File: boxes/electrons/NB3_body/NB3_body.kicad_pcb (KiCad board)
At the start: 2 copper layers, 200 x 199.5 mm, 18 parts, among them J1 Conn_02x05_Counter_Clockwise, J10 Conn_02x03_Top_Bottom, J11 Conn_02x03_Top_Bottom, J12 Conn_02x03_Top_Bottom, J13 JST ZH 6-way Socket, J14 JST ZH 6-way Socket, J2 Conn_02x05_Counter_Clockwise, J3 Conn_02x05_Counter_Clockwise, J4 Conn_02x05_Counter_Clockwise, J5 Conn_02x05_Counter_Clockwise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

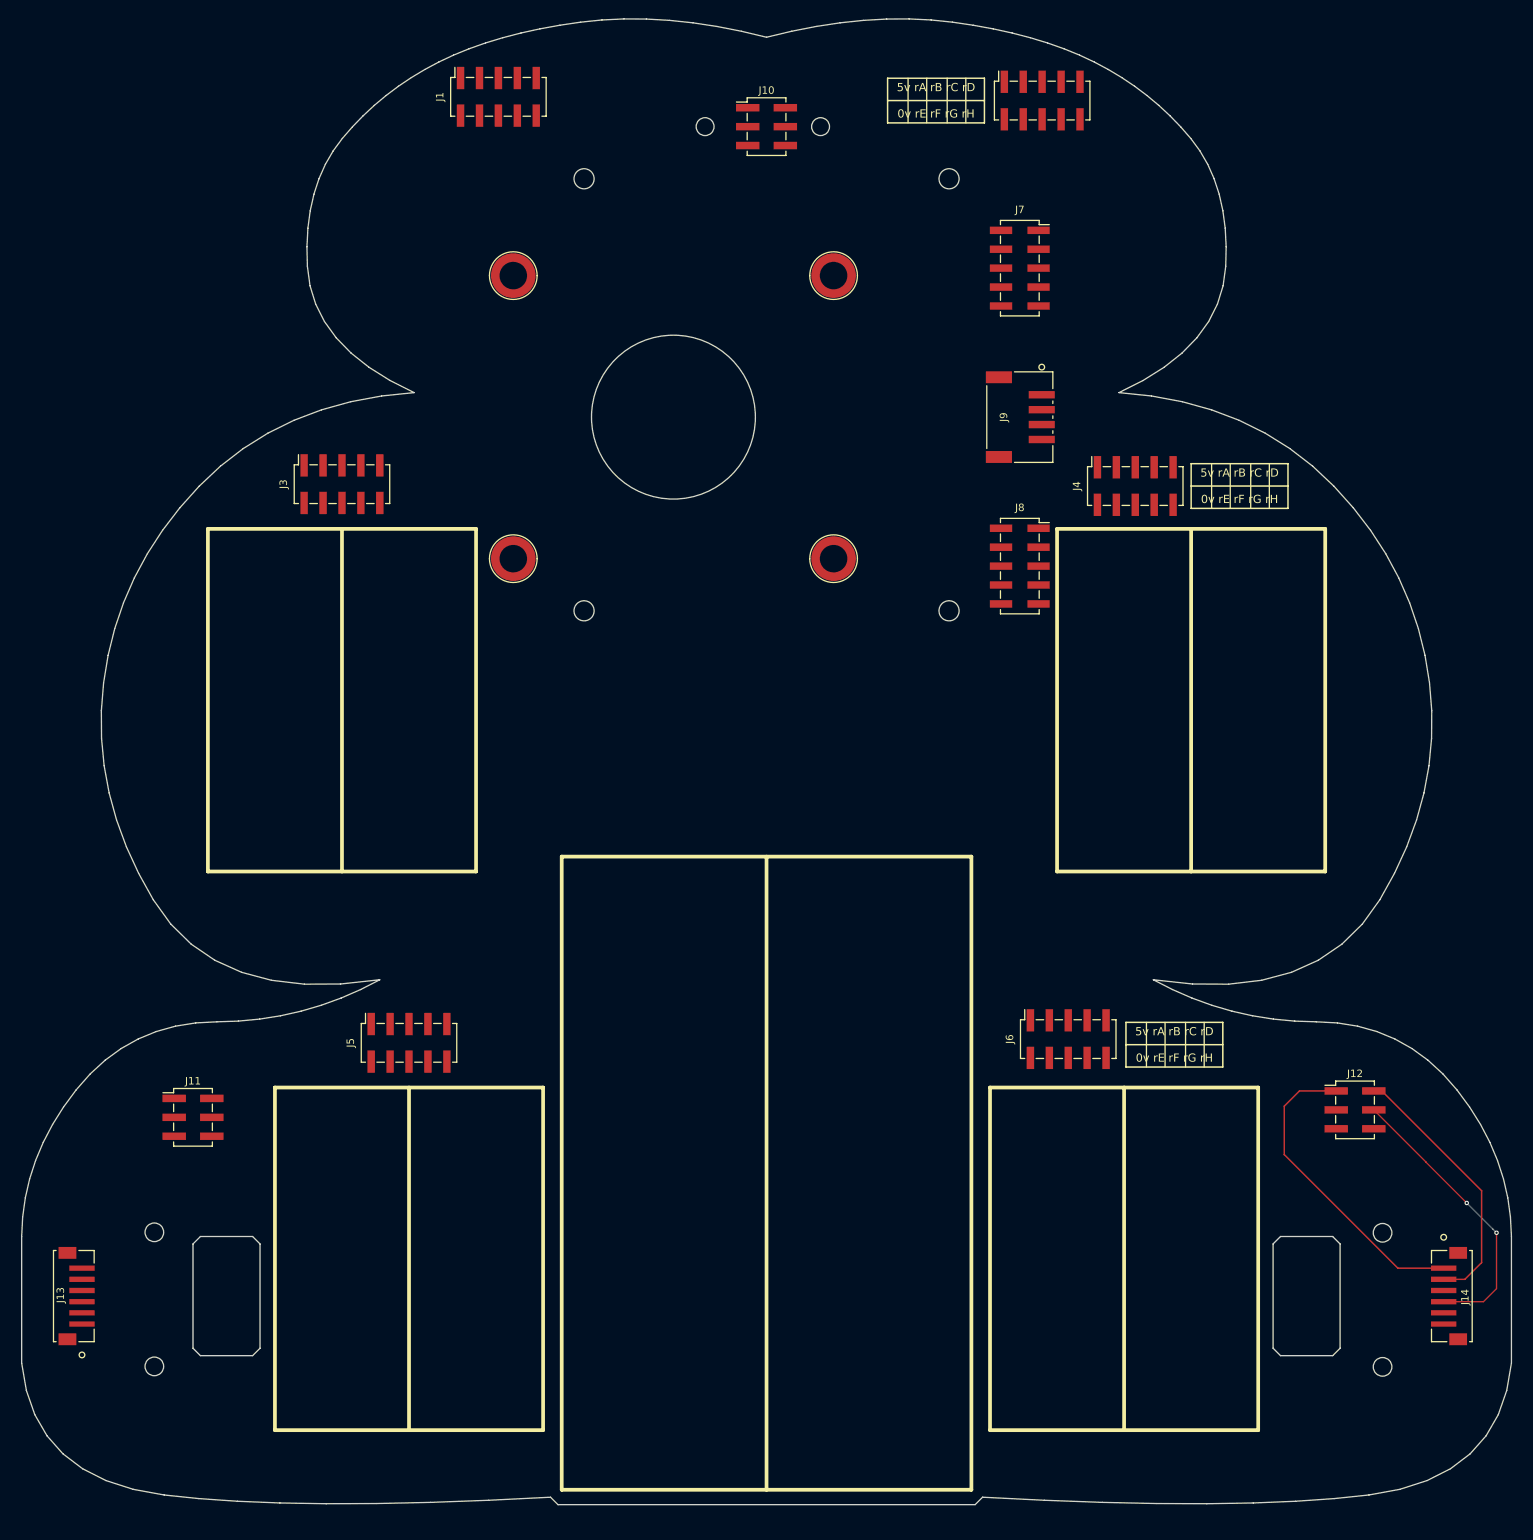
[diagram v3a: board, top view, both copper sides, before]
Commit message: NB3 pcb design tweaks
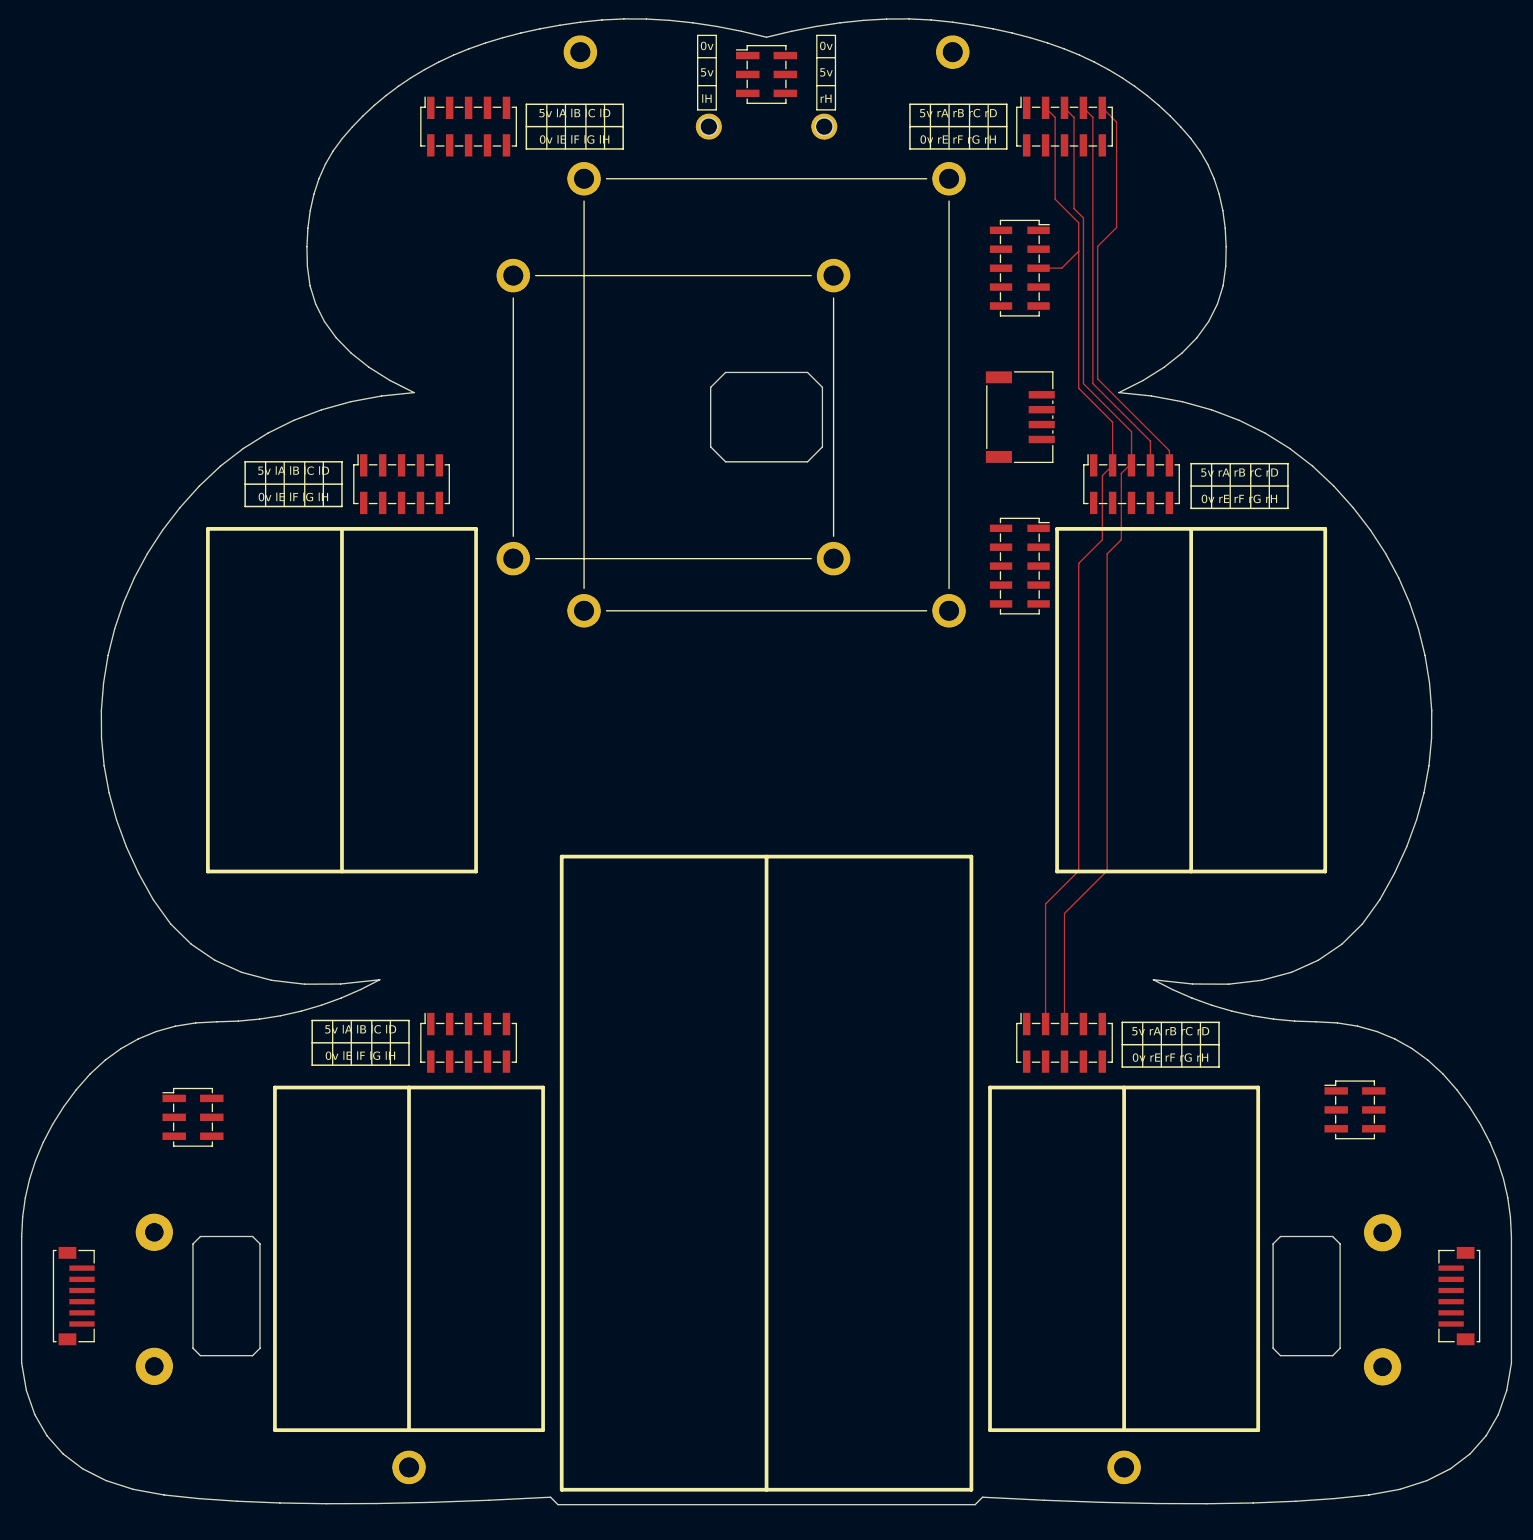
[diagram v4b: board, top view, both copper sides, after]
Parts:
- added H10: MountingHole, MountingHole:MountingHole_2.5mm_Pad, F.Cu at (207.2, 186.5)
- added H11: MountingHole, MountingHole:MountingHole_2.5mm_Pad, F.Cu at (42.3, 204.4)
- added H12: MountingHole, MountingHole:MountingHole_2.5mm_Pad, F.Cu at (207.2, 204.5)
- added H13: MountingHole, MountingHole:MountingHole_2.7mm_M2.5_ISO7380_Pad, F.Cu at (99.5, 28.0)
- added H14: MountingHole, MountingHole:MountingHole_2.7mm_M2.5_ISO7380_Pad, F.Cu at (149.5, 28.0)
- added H15: MountingHole, MountingHole:MountingHole_2.7mm_M2.5_ISO7380_Pad, F.Cu at (76.5, 218.0)
- added H16: MountingHole, MountingHole:MountingHole_2.7mm_M2.5_ISO7380_Pad, F.Cu at (172.5, 218.0)
- added H17: MountingHole, MountingHole:MountingHole_2.2mm_M2_ISO7380_Pad, F.Cu at (116.8, 38.0)
- added H18: MountingHole, MountingHole:MountingHole_2.2mm_M2_ISO7380_Pad, F.Cu at (132.2, 38.0)
- added H5: MountingHole, MountingHole:MountingHole_2.7mm_M2.5_ISO7380_Pad, F.Cu at (100.0, 45.0)
- added H6: MountingHole, MountingHole:MountingHole_2.7mm_M2.5_ISO7380_Pad, F.Cu at (149.0, 45.0)
- added H7: MountingHole, MountingHole:MountingHole_2.7mm_M2.5_ISO7380_Pad, F.Cu at (100.0, 103.0)
- added H8: MountingHole, MountingHole:MountingHole_2.7mm_M2.5_ISO7380_Pad, F.Cu at (149.0, 103.0)
- added H9: MountingHole, MountingHole:MountingHole_2.5mm_Pad, F.Cu at (42.3, 186.4)
- H1, H2, H3, H4: value Standoff_SMT_5H_M2.5_9774050151R -> MountingHole; footprint NB3_body:Standoff_SMT_5H_M2.5_9774050151R -> MountingHole:MountingHole_2.7mm_M2.5_ISO7380_Pad
- moved J3 8.00 mm to (75.5, 86.0)
- moved J5 8.00 mm to (84.5, 161.0)
- moved J10 7.00 mm to (124.5, 31.0)
- moved J1 5.66 mm to (84.5, 38.0)
- moved J2 4.61 mm to (164.5, 38.0)
- moved J14 1.00 mm to (217.5, 195.0)
- moved J6 0.71 mm to (164.5, 161.0)
- moved J4 0.56 mm to (173.5, 86.0)
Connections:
- J1 pad 10: GND -> /LH
- J1 pad 2: /LA -> GND
- J1 pad 3: /LB -> /LA
- J1 pad 4: /LC -> /LE
- J1 pad 5: /LD -> /LB
- J1 pad 6: /LH -> /LF
- J1 pad 7: /LG -> /LC
- J1 pad 8: /LF -> /LG
- J1 pad 9: /LE -> /LD
- J10 pad 2: +5V -> GND
- J10 pad 3: /LH -> +5V
- J10 pad 4: GND -> +5V
- J10 pad 5: +5V -> /LH
- J11 pad 2: /LE+ -> /LE B
- J11 pad 3: /LE A -> /LE+
- J11 pad 4: /LE B -> /LE-
- J11 pad 5: /LE- -> /LE A
- J12 pad 2: /RE+ -> /RE B
- J12 pad 3: /RE A -> /RE+
- J12 pad 4: /RE B -> /RE-
- J12 pad 5: /RE- -> /RE A
- J2 pad 10: GND -> /RH
- J2 pad 2: /RA -> GND
- J2 pad 3: /RB -> /RA
- J2 pad 4: /RC -> /RE
- J2 pad 5: /RD -> /RB
- J2 pad 6: /RH -> /RF
- J2 pad 7: /RG -> /RC
- J2 pad 8: /RF -> /RG
- J2 pad 9: /RE -> /RD
- J3 pad 10: GND -> /LH
- J3 pad 2: /LA -> GND
- J3 pad 3: /LB -> /LA
- J3 pad 4: /LC -> /LE
- J3 pad 5: /LD -> /LB
- J3 pad 6: /LH -> /LF
- J3 pad 7: /LG -> /LC
- J3 pad 8: /LF -> /LG
- J3 pad 9: /LE -> /LD
- J4 pad 10: GND -> /RH
- J4 pad 2: /RA -> GND
- J4 pad 3: /RB -> /RA
- J4 pad 4: /RC -> /RE
- J4 pad 5: /RD -> /RB
- J4 pad 6: /RH -> /RF
- J4 pad 7: /RG -> /RC
- J4 pad 8: /RF -> /RG
- J4 pad 9: /RE -> /RD
- J5 pad 10: GND -> /LH
- J5 pad 2: /LA -> GND
- J5 pad 3: /LB -> /LA
- J5 pad 4: /LC -> /LE
- J5 pad 5: /LD -> /LB
- J5 pad 6: /LH -> /LF
- J5 pad 7: /LG -> /LC
- J5 pad 8: /LF -> /LG
- J5 pad 9: /LE -> /LD
- J6 pad 10: GND -> /RH
- J6 pad 2: /RA -> GND
- J6 pad 3: /RB -> /RA
- J6 pad 4: /RC -> /RE
- J6 pad 5: /RD -> /RB
- J6 pad 6: /RH -> /RF
- J6 pad 7: /RG -> /RC
- J6 pad 8: /RF -> /RG
- J6 pad 9: /RE -> /RD
- J7 pad 1: +5V -> GND
- J7 pad 10: GND -> /LC
- J7 pad 3: /LA -> GND
- J7 pad 4: /LB -> +5V
- J7 pad 5: /LC -> /RA
- J7 pad 6: /RC -> /LA
- J7 pad 8: /RA -> /LB
- J7 pad 9: GND -> /RC
- J8 pad 1: /LD -> /RD
- J8 pad 10: /RD -> /LH
- J8 pad 2: /LE -> /LD
- J8 pad 3: /LF -> /RE
- J8 pad 4: /LG -> /LE
- J8 pad 5: /LH -> /RF
- J8 pad 6: /RH -> /LF
- J8 pad 8: /RF -> /LG
- J8 pad 9: /RE -> /RH
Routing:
- net /RA: track 0.00 -> 136.8 mm
- net /RB: track 0.00 -> 130.6 mm
- net /RD: track 0.00 -> 53.8 mm
- net /RC: track 0.00 -> 51.7 mm
- net /RM+: track 42.0 -> 0.00 mm
- net /RE B: track 38.6 -> 0.00 mm, vias 2 -> 0
- net /RE+: track 35.7 -> 0.00 mm
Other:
- outline, holes or cut-outs redrawn
- board text added: "0v 5v lH"
- board text added: "0v 5v rH"
- board text added: "5v lA lB lC lD 0v lE lF lG lH"

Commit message: Work on NB£_body PCB
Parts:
- added H19: MountingHole, MountingHole:MountingHole_2.7mm_M2.5_ISO7380_Pad, F.Cu at (39.5, 118.0)
- added H20: MountingHole, MountingHole:MountingHole_2.7mm_M2.5_ISO7380_Pad, F.Cu at (209.5, 118.0)
- moved H13 5.10 mm to (94.5, 29.0)
- moved H14 5.10 mm to (154.5, 29.0)
- moved J11 3.61 mm to (45.5, 168.0), turned to 180 degrees
- moved J12 2.00 mm to (203.5, 168.0), turned to 180 degrees
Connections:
- J1 pad 1: +5V -> /LA
- J1 pad 10: /LH -> GND
- J1 pad 2: GND -> /LE
- J1 pad 3: /LA -> /LB
- J1 pad 4: /LE -> /LF
- J1 pad 5: /LB -> /LC
- J1 pad 6: /LF -> /LG
- J1 pad 7: /LC -> /LD
- J1 pad 8: /LG -> /LH
- J1 pad 9: /LD -> +5V
- J12 pad 1: /RM+ -> /RE B
- J12 pad 2: /RE B -> /RM+
- J12 pad 3: /RE+ -> /RE-
- J12 pad 4: /RE- -> /RE+
- J12 pad 5: /RE A -> /RM-
- J12 pad 6: /RM- -> /RE A
- J13 pad 1: /LM+ -> /LM-
- J13 pad 2: /LE+ -> /LE-
- J13 pad 3: /LE A -> /LE B
- J13 pad 4: /LE B -> /LE A
- J13 pad 5: /LE- -> /LE+
- J13 pad 6: /LM- -> /LM+
- J3 pad 1: +5V -> /LA
- J3 pad 10: /LH -> GND
- J3 pad 2: GND -> /LE
- J3 pad 3: /LA -> /LB
- J3 pad 4: /LE -> /LF
- J3 pad 5: /LB -> /LC
- J3 pad 6: /LF -> /LG
- J3 pad 7: /LC -> /LD
- J3 pad 8: /LG -> /LH
- J3 pad 9: /LD -> +5V
- J5 pad 1: +5V -> /LA
- J5 pad 10: /LH -> GND
- J5 pad 2: GND -> /LE
- J5 pad 3: /LA -> /LB
- J5 pad 4: /LE -> /LF
- J5 pad 5: /LB -> /LC
- J5 pad 6: /LF -> /LG
- J5 pad 7: /LC -> /LD
- J5 pad 8: /LG -> /LH
- J5 pad 9: /LD -> +5V
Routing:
- net /LH: track 0.00 -> 270.0 mm, vias 0 -> 6
- net /LE: track 0.00 -> 246.2 mm, vias 0 -> 5
- net /LF: track 0.00 -> 241.0 mm, vias 0 -> 5
- net /LG: track 0.00 -> 235.7 mm, vias 0 -> 5
- net /LA: track 0.00 -> 231.2 mm, vias 0 -> 4
- net /LB: track 0.00 -> 228.9 mm, vias 0 -> 4
- net /LC: track 0.00 -> 226.7 mm, vias 0 -> 4
- net /LD: track 0.00 -> 226.0 mm, vias 0 -> 6
- net /RH: track 0.00 -> 208.9 mm, vias 0 -> 4
- net /RG: track 0.00 -> 159.1 mm, vias 0 -> 3
- net /RF: track 0.00 -> 156.2 mm, vias 0 -> 3
- net /RE: track 0.00 -> 153.4 mm, vias 0 -> 3
- net /RD: track 53.8 -> 168.7 mm, vias 0 -> 4
- net /RC: track 51.7 -> 159.7 mm, vias 0 -> 4
- net GND: track 0.00 -> 54.0 mm, vias 0 -> 13
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- added copper zone on F.Cu, net +5V
- added copper zone on B.Cu, net GND
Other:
- outline, holes or cut-outs redrawn
- board text added: "0v 0v rA rB rC 5v 5v lA lB lC"
- board text added: "5v 5v 0v 0v"
- board text added: "AA Battery Pack"
- board text added: "NiMH Battery Pack"
- board text added: "lA lB lC lD 5v lE lF lG lH 0v"
- board text added: "rD rE rF rG rH lD lE lF lG lH"
- board text removed: "5v lA lB lC lD 0v lE lF lG lH"

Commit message: Finished NB3_body PCB (pre-Fab)
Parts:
- added G***: LOGO, NB3_body:Logo_NBB_15mm, F.Cu at (124.5, 116.0)
- added G***: LOGO, NB3_body:Logo_VK_15mm, B.Cu at (124.5, 123.0)
- moved H15 0.50 mm to (76.5, 217.5)
- moved H16 0.50 mm to (172.5, 217.5)
- turned J11 to 0 degrees
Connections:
- J13 pad 1: /LM- -> /LM+
- J13 pad 2: /LE- -> /LE+
- J13 pad 3: /LE B -> /LE A
- J13 pad 4: /LE A -> /LE B
- J13 pad 5: /LE+ -> /LE-
- J13 pad 6: /LM+ -> /LM-
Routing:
- net /LE B: track 36.6 -> 47.8 mm
- net /LE A: track 47.8 -> 36.6 mm
- net /LM-: track 47.5 -> 37.3 mm
- net /LM+: track 37.3 -> 47.5 mm
- net /LE-: track 42.4 -> 43.0 mm
- net /LE+: track 43.0 -> 42.4 mm
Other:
- board text added: "FOREBRAIN"
- board text added: "HINDBRAIN"
- board text added: "MIDBRAIN"
- board text added: "MUSCLES"
- board text added: "NB3_body Rev 0.0.1"
- board text added: "POWER"
- board text added: "SPINAL CORD"
- board text added: "lM+ lEb lE+ lE- lEa lM-"
- board text added: "rEa rM- rE+ rE- rM+ rEb"
- board text added: "{dblquote}No Black Boxes{dblquote}"
